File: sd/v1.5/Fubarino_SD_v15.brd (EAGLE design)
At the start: 71.1 x 25.4 mm, 38 parts, among them IC1 PIC32MX440F256H-80I/PT, IC2 MCP1702T-3302E/MB, J1 MICRO_SD_CARD_SOCKET, J2 M28USEPIN1, J3 M28NOPIN1, J8 USB-5PIN, Q1 8MHz, Q2 32.768 KHz

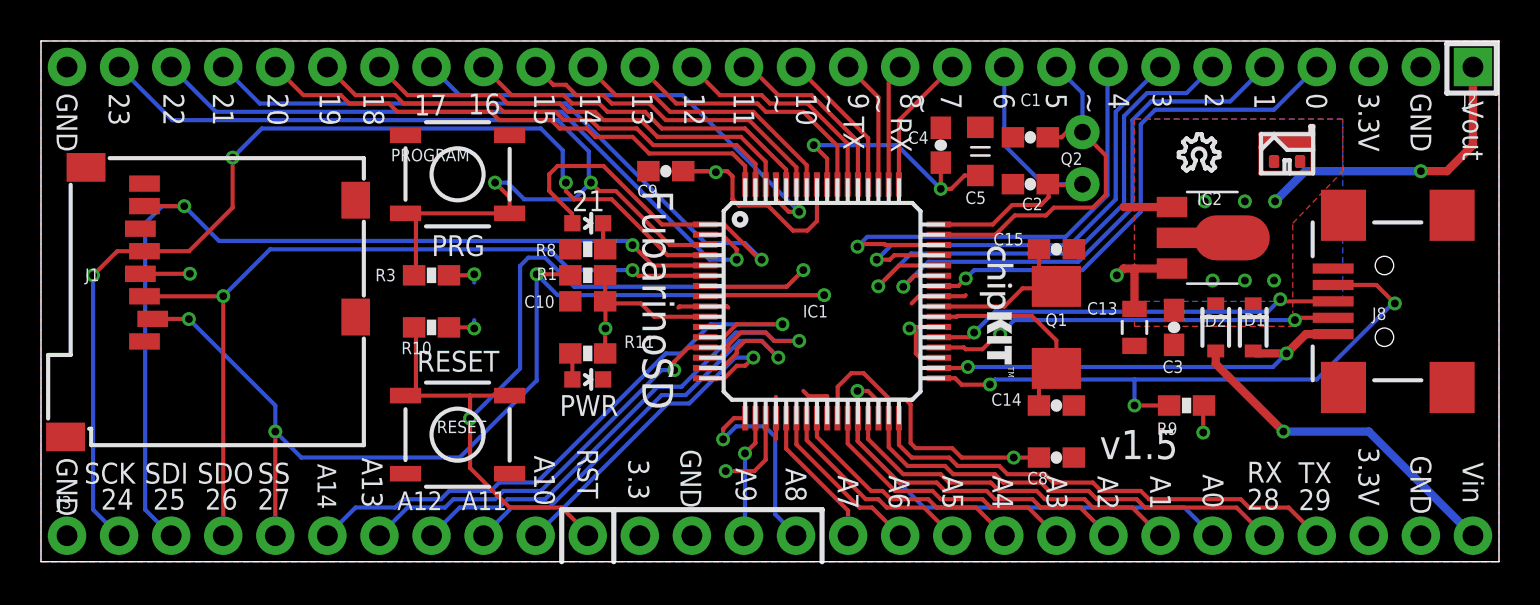
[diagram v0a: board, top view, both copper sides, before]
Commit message: Created PIC32MX795F512H symbol, and updated schematic with it. Also had to re-do nets to CPU on layout because Eagle reasons.
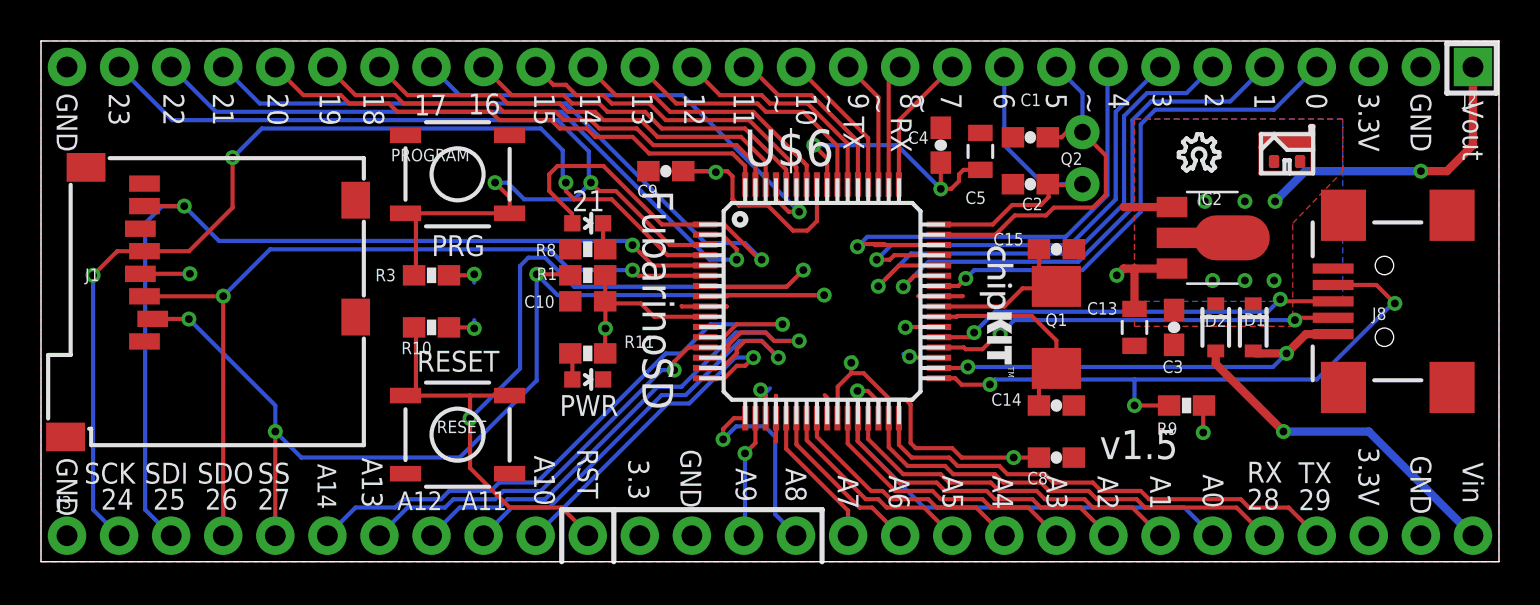
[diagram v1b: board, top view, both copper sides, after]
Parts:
- removed IC1: PIC32MX440F256H-80I/PT, microchip:TQFP64-10X10
- added U$6: PIC32MX795F512H-I/PT, SchmalzHaus:TQFP64-10X10
- C5: device SchmalzHaus:CAP_0805 -> SchmalzHaus:0805
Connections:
- net !MCLR!: now also U$6.7; no longer IC1.7
- net 3.3V: now also U$6.10, U$6.19, U$6.26, U$6.35, U$6.38, U$6.57; no longer IC1.10, IC1.19, IC1.26, IC1.35, IC1.38, IC1.57
- net D+: now also U$6.37; no longer IC1.37
- net D-: now also U$6.36; no longer IC1.36
- net GND: now also U$6.20, U$6.25, U$6.41, U$6.9; no longer IC1.20, IC1.25, IC1.41, IC1.9
- net N$110: now also U$6.56; no longer IC1.56
- net OSC1: now also U$6.39; no longer IC1.39
- net OSC2: now also U$6.40; no longer IC1.40
- net RB0: now also U$6.16; no longer IC1.16
- net RB1: now also U$6.15; no longer IC1.15
- net RB10: now also U$6.23; no longer IC1.23
- net RB11: now also U$6.24; no longer IC1.24
- net RB12: now also U$6.27; no longer IC1.27
- net RB13: now also U$6.28; no longer IC1.28
- net RB14: now also U$6.29; no longer IC1.29
- net RB15: now also U$6.30; no longer IC1.30
- net RB2: now also U$6.14; no longer IC1.14
- net RB3: now also U$6.13; no longer IC1.13
- net RB4: now also U$6.12; no longer IC1.12
- net RB6: now also U$6.17; no longer IC1.17
- net RB7: now also U$6.18; no longer IC1.18
- net RB8: now also U$6.21; no longer IC1.21
- net RB9: now also U$6.22; no longer IC1.22
- net RC13: now also U$6.47; no longer IC1.47
- net RC14: now also U$6.48; no longer IC1.48
- net RD0: now also U$6.46; no longer IC1.46
- net RD1: now also U$6.49; no longer IC1.49
- net RD10: now also U$6.44; no longer IC1.44
- net RD11: now also U$6.45; no longer IC1.45
- net RD2: now also U$6.50; no longer IC1.50
- net RD3: now also U$6.51; no longer IC1.51
- net RD4: now also U$6.52; no longer IC1.52
- net RD5: now also U$6.53; no longer IC1.53
- net RD6: now also U$6.54; no longer IC1.54
- net RD7: now also U$6.55; no longer IC1.55
- net RD8: now also U$6.42; no longer IC1.42
- net RD9: now also U$6.43; no longer IC1.43
- net RE0: now also U$6.60; no longer IC1.60
- net RE1: now also U$6.61; no longer IC1.61
- net RE2: now also U$6.62; no longer IC1.62
- net RE3: now also U$6.63; no longer IC1.63
- net RE4: now also U$6.64; no longer IC1.64
- net RE5: now also U$6.1; no longer IC1.1
- net RE6: now also U$6.2; no longer IC1.2
- net RE7: now also U$6.3; no longer IC1.3
- net RF0: now also U$6.58; no longer IC1.58
- net RF1: now also U$6.59; no longer IC1.59
- net RF4: now also U$6.31; no longer IC1.31
- net RF5: now also U$6.32; no longer IC1.32
- net RG6: now also U$6.4; no longer IC1.4
- net RG7: now also U$6.5; no longer IC1.5
- net RG8: now also U$6.6; no longer IC1.6
- net RG9: now also U$6.8; no longer IC1.8
- net USBID: now also U$6.33; no longer IC1.33
- net VBUS: now also U$6.34; no longer IC1.34
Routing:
- net 3.3V: track 55.5 -> 53.7 mm, vias 10 -> 12
- net GND: track 12.1 -> 10.2 mm
- net RD0: track 23.5 -> 24.1 mm
